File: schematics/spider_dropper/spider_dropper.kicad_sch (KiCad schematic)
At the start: 15 parts, among them J1 12V DC, J2 Sensor, J3 Motor, Q1 2N3904, Q2 TIP120, SW1 ZX40E10C01

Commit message: Changed PIR connector to JST XH, which is keyed and holds securely.
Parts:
- J2: footprint Connector_PinSocket_2.54mm:PinSocket_1x03_P2.54mm_Vertical -> Connector_JST:JST_XH_B3B-XH-A_1x03_P2.50mm_Vertical
- UX1: footprint aid_Modules:HC-SR312_PIR_Motion_Sensor -> Connector_JST:JST_XH_B3B-XH-A_1x03_P2.50mm_Vertical
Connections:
- net GND: now also J2.1 (Pin_1); no longer J2.3 (Pin_3)
- net at D1.1 (K), F1.2, J3.1 (Pin_1)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: now also J2.3 (Pin_3); no longer J2.1 (Pin_1)
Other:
- moved on the sheet: J2
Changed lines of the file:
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@@
 	(symbol
 		(lib_id "Connector:Conn_01x03_Socket")
-		(at 109.22 82.55 0)
-		(mirror y)
+		(at 109.22 82.55 180)
 		(unit 1)
 		(exclude_from_sim no)
@@
 		(dnp no)
 		(property "Reference" "J2"
-			(at 109.22 74.676 0)
+			(at 109.22 90.424 0)
 			(effects
 				(font
@@
 		)
 		(property "Value" "Sensor"
-			(at 109.22 77.1003 0)
+			(at 109.22 87.9997 0)
 			(effects
 				(font
@@
 			)
 		)
-		(property "Footprint" "Connector_PinSocket_2.54mm:PinSocket_1x03_P2.54mm_Vertical"
+		(property "Footprint" "Connector_JST:JST_XH_B3B-XH-A_1x03_P2.50mm_Vertical"
 			(at 109.22 82.55 0)
 			(effects
@@
 			)
 		)
-		(property "Footprint" "aid_Modules:HC-SR312_PIR_Motion_Sensor"
+		(property "Footprint" "Connector_JST:JST_XH_B3B-XH-A_1x03_P2.50mm_Vertical"
 			(at 52.07 82.55 0)
 			(effects

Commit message: Switched the JST XH footprint to one with hole for "boss".
The boss is for alignment and possibly additional support.  This
footprint is compatible with the connector that doesn't have a boss.
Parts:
- J2: footprint Connector_JST:JST_XH_B3B-XH-A_1x03_P2.50mm_Vertical -> Connector_JST:JST_XH_B3B-XH-AM_1x03_P2.50mm_Vertical
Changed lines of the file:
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@@
 			)
 		)
-		(property "Footprint" "Connector_JST:JST_XH_B3B-XH-A_1x03_P2.50mm_Vertical"
+		(property "Footprint" "Connector_JST:JST_XH_B3B-XH-AM_1x03_P2.50mm_Vertical"
 			(at 109.22 82.55 0)
 			(effects

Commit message: Tried to do circuit simulation in KiCad.  Not working yet.
The Spice models are from manufacturer OnSemi's website.
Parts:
- Q1: footprint Package_TO_SOT_THT:TO-92_HandSolder -> Package_TO_SOT_THT:TO-92L_HandSolder

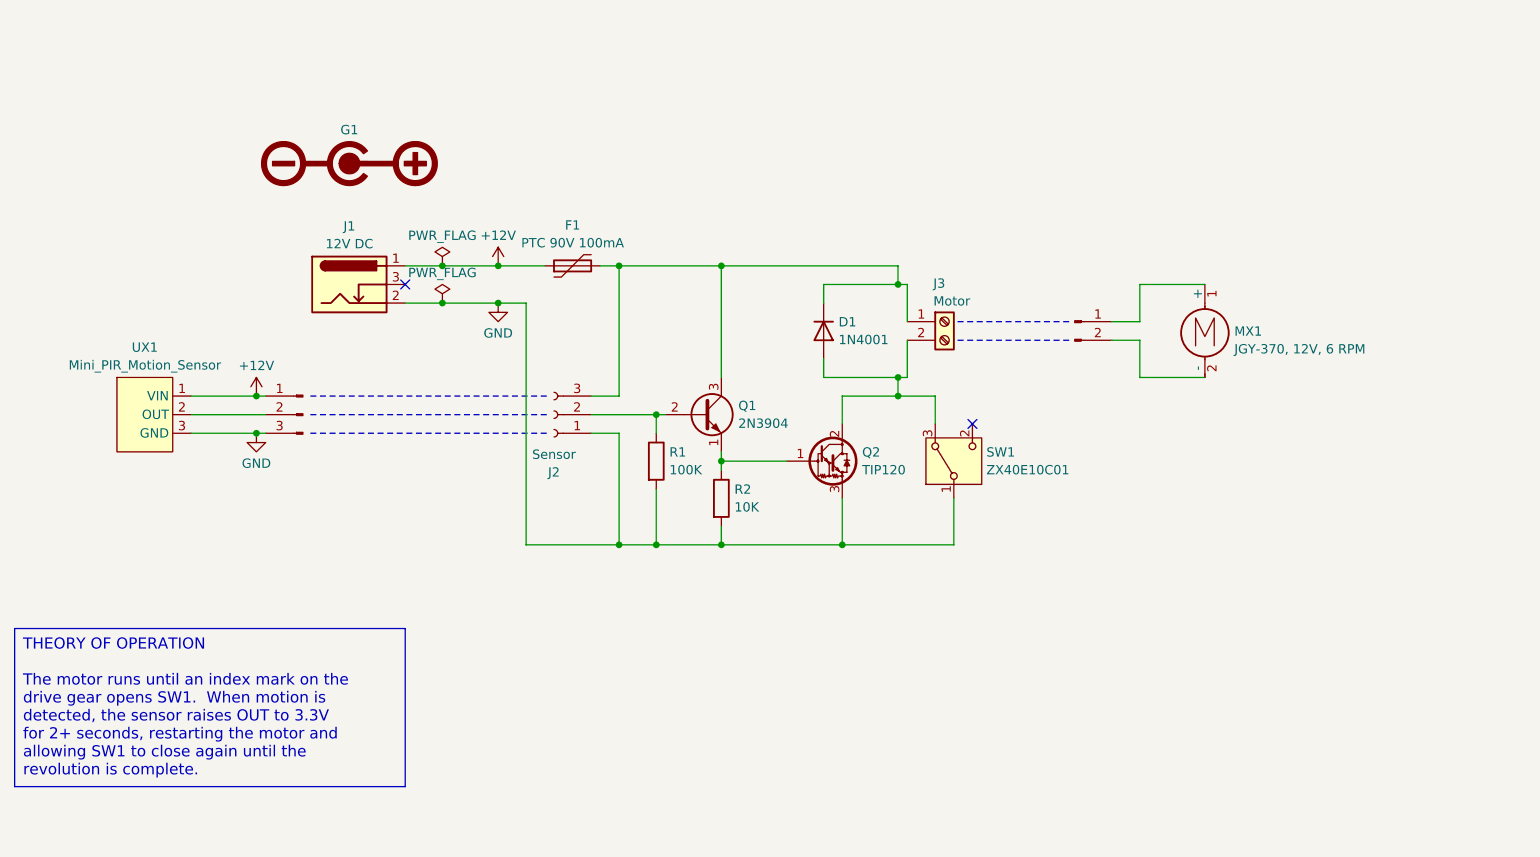
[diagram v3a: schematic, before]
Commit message: Added current-limiting resistor to base of Q2.
With the thermal camera, I happened to notice that Q1 was heating up
more than I expected.  When on, it was passing almost 11mA.  Within
spec, but way more than necessary to turn on Q2.  Added a current
limited resistor to the base of Q2 dropped the current (and power)
through Q1 to less than 1mA.

Made additional layout tweaks to PCB and updated markings to Rev C.
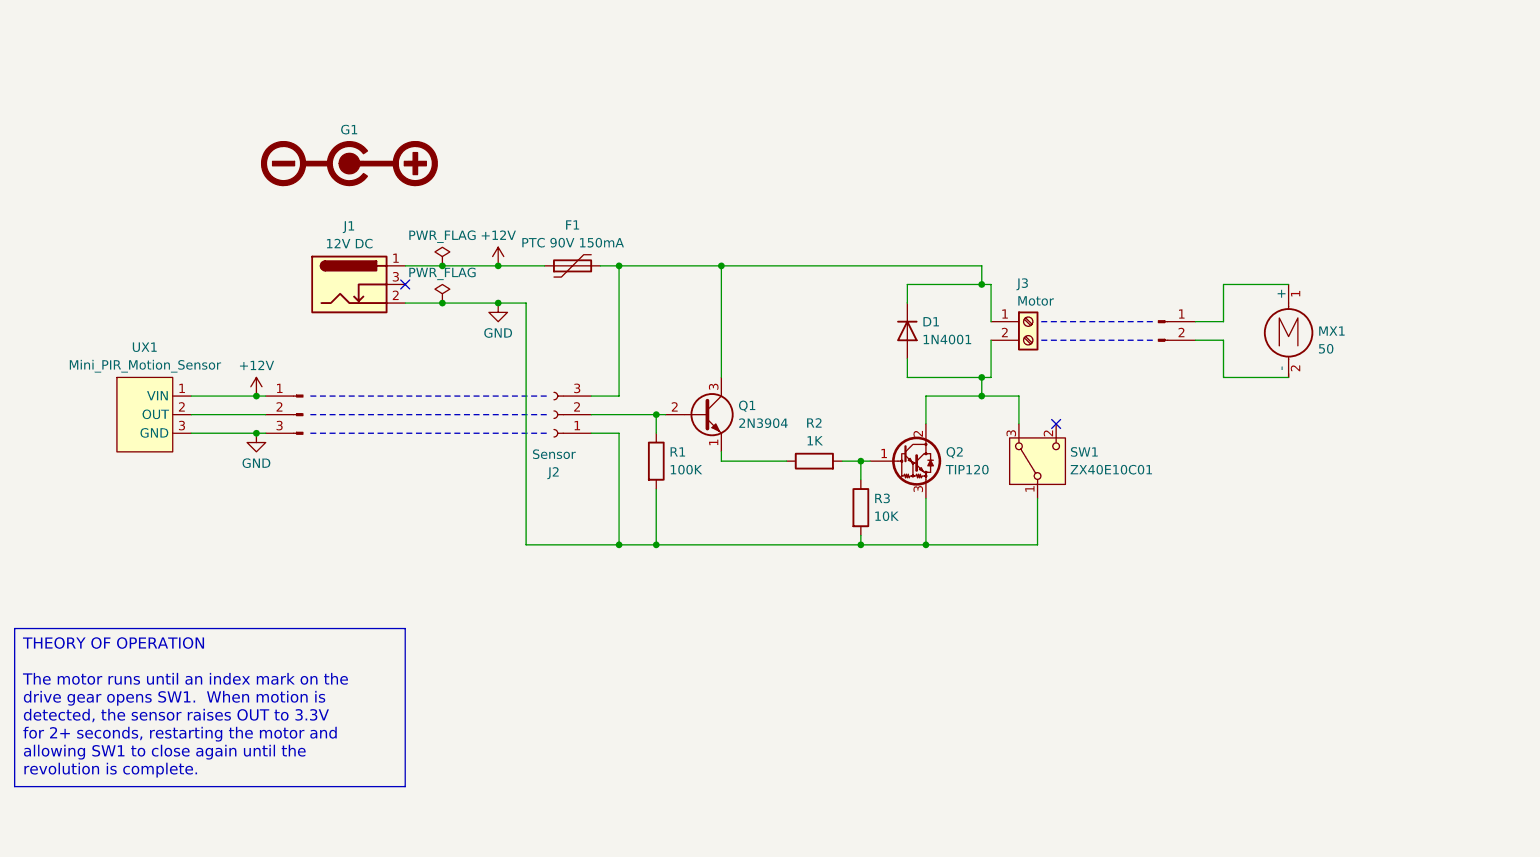
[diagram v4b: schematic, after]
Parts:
- added R2: 1K, Resistor_THT:R_Axial_DIN0207_L6.3mm_D2.5mm_P7.62mm_Horizontal, symbol Device:R
- F1: value PTC 90V 100mA -> PTC 90V 150mA
- MX1: value JGY-370, 12V, 6 RPM -> 50
- renumbered R2 to R3
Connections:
- net at Q2.1 (B), R3.1: now also R2.2; no longer Q1.1 (E)
- new net: Q1.1 (E), R2.1
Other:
- moved on the sheet: D1, J3, MX1, Q2, R3, SW1

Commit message: Redesign of slightly smarter PCB.
Simplified by using a MOSFET, which requires fewer parts and runs the
motor more efficiently.  Since I'm also working on a re-do of the
printed parts, I went ahead and changed the layout and mounting options
for the board.  That makes the new PCB incompatible with the old
mechanical design.
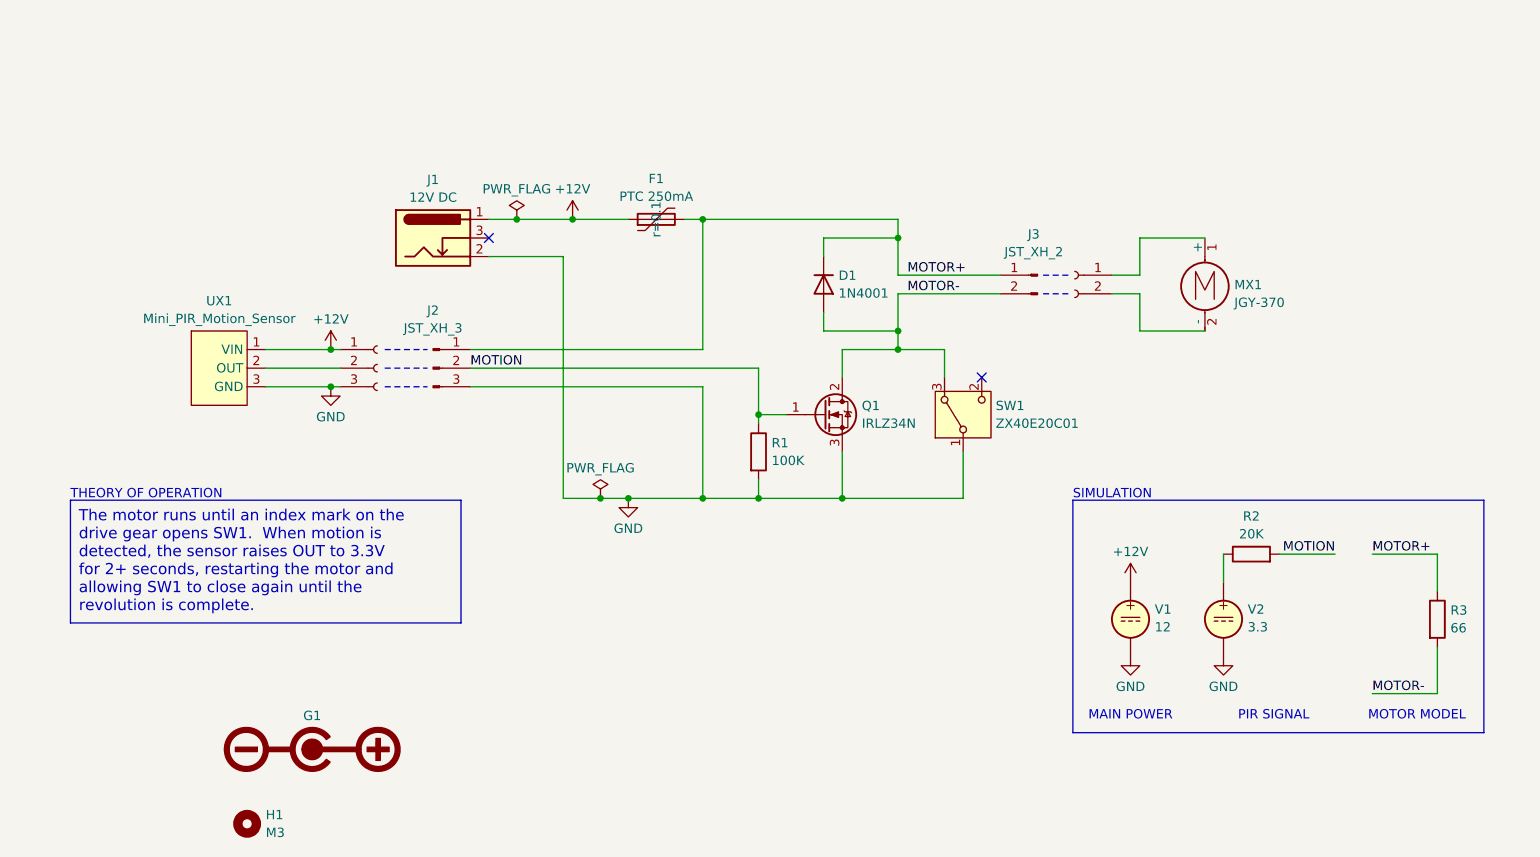
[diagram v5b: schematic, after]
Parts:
- removed J3: Motor, aid_Connector:CUI_TB007-508_01x02_THT_Screw_Terminal_Block, symbol Connector:Screw_Terminal_01x02
- removed Q1: 2N3904, Package_TO_SOT_THT:TO-92L_HandSolder, symbol Transistor_BJT:2N3904
- removed Q2: TIP120, Package_TO_SOT_THT:TO-220-3_Horizontal_TabDown, symbol Transistor_BJT:TIP120
- added H1: M3, MountingHole:MountingHole_3.2mm_M3, symbol Mechanical:MountingHole
- added J3: JST_XH_2, Connector_JST:JST_XH_B2B-XH-AM_1x02_P2.50mm_Vertical, symbol Connector:Conn_01x02_Pin
- added Q1: IRLZ34N, Package_TO_SOT_THT:TO-220-3_Horizontal_TabDown, symbol Transistor_FET:IRLZ34N
- added V1: 12, symbol Simulation_SPICE:VDC
- added V2: 3.3, symbol Simulation_SPICE:VDC
- F1: value PTC 90V 150mA -> PTC 250mA
- J1: footprint Connector_BarrelJack:BarrelJack_CUI_PJ-102AH_Horizontal -> aid_Connector:BarrelJack_SameSky(CUI)_PJ-044AH
- J2: value Sensor -> JST_XH_3; symbol Connector:Conn_01x03_Socket -> Connector:Conn_01x03_Pin
- JX1: value Conn_01x03_Pin -> JST_XS_3; symbol Connector:Conn_01x03_Pin -> Connector:Conn_01x03_Socket; now left out of the parts list
- JX2: value Conn_01x02_Pin -> JST_XH_2; symbol Connector:Conn_01x02_Pin -> Connector:Conn_01x02_Socket
- MX1: value 50 -> JGY-370
- R2: value 1K -> 20K; footprint Resistor_THT:R_Axial_DIN0207_L6.3mm_D2.5mm_P7.62mm_Horizontal -> (none); now left out of the parts list
- R3: value 10K -> 66; footprint Resistor_THT:R_Axial_DIN0207_L6.3mm_D2.5mm_P7.62mm_Horizontal -> (none); now left out of the parts list
- SW1: value ZX40E10C01 -> ZX40E20C01
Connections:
- net +12V: now also V1.1
- net GND: now also J2.3 (Pin_3), Q1.3 (S), V1.2, V2.2; no longer J2.1 (Pin_1), R3.2
- net MOTION: now reaches R2.2
- net MOTION: now also J2.2 (Pin_2), R1.1, Q1.1 (G); no longer R3.1
- net MOTOR-: now reaches D1.2 (A), SW1.3 (A)
- net MOTOR-: now also R3.2, J3.2 (Pin_2), Q1.2 (D)
- net MOTOR+: now reaches D1.1 (K), F1.2
- net MOTOR+: now also J2.1 (Pin_1), R3.1, J3.1 (Pin_1); no longer J2.3 (Pin_3)
- net at R2.1: now also V2.1
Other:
- note added: "MAIN POWER"
- note added: "MOTOR MODEL"
- note added: "PIR SIGNAL"
- note added: "SIMULATION"
- note added: "THEORY OF OPERATION"
- moved on the sheet: D1, F1, G1, J1, MX1, R1, SW1, UX1

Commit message: I think I'm ready to order Rev. D PCBs.
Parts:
- J2: renamed from J1; value 12V DC -> PJ-044AH
- renumbered J2 to J1, R2 to RX1, R3 to RX2
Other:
- note added: "ERC"
- note added: "GRAPHICS"
- note added: "HARDWARE"
- moved on the sheet: D1, F1, G1, H1, J2, J3, MX1, Q1, R1, RX1, RX2, SW1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
